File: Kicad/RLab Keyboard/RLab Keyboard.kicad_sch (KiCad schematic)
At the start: 75 parts, among them J1 Conn_01x01_Pin, J10 Conn_01x01_Pin, J11 Conn_01x01_Pin, J12 Conn_01x01_Pin, J13 Conn_01x04, J14 Conn_01x07, J15 Conn_01x03, J16 AudioJack3_Switch, J17 Conn_01x03, J18 Conn_01x03, J19 Conn_01x09, J2 Conn_01x01_Pin, J3 Conn_01x01_Pin, J4 Conn_01x01_Pin, J5 Conn_01x01_Pin, J6 Conn_01x01_Pin, J7 Conn_01x01_Pin, J8 Conn_01x01_Pin, J9 Conn_01x01_Pin, SW1 SW_MEC_5G, SW2 SW_MEC_5G, U1 MPR121QR2, U2 LP5907MFX-3.3, U3 74LVC1G17, U4 PCM5102, U5 LM386

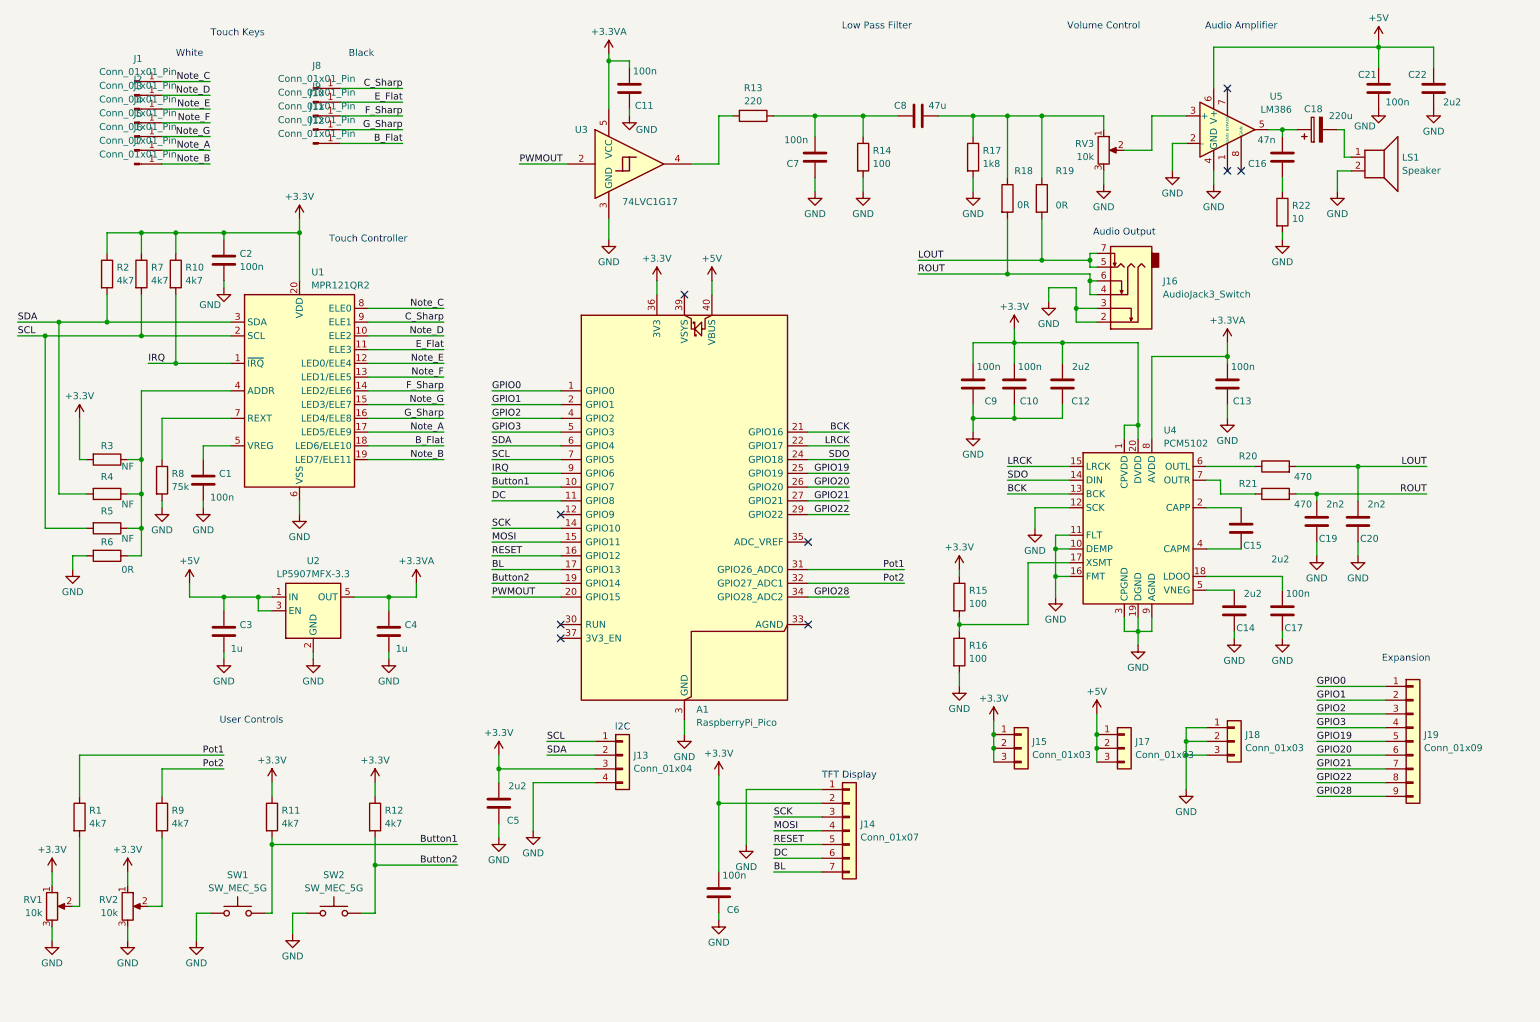
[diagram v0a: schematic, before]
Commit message: Initial submit of version 1.2
Update to layout of Kicad files for new user interface
Added circuit Python test firmware
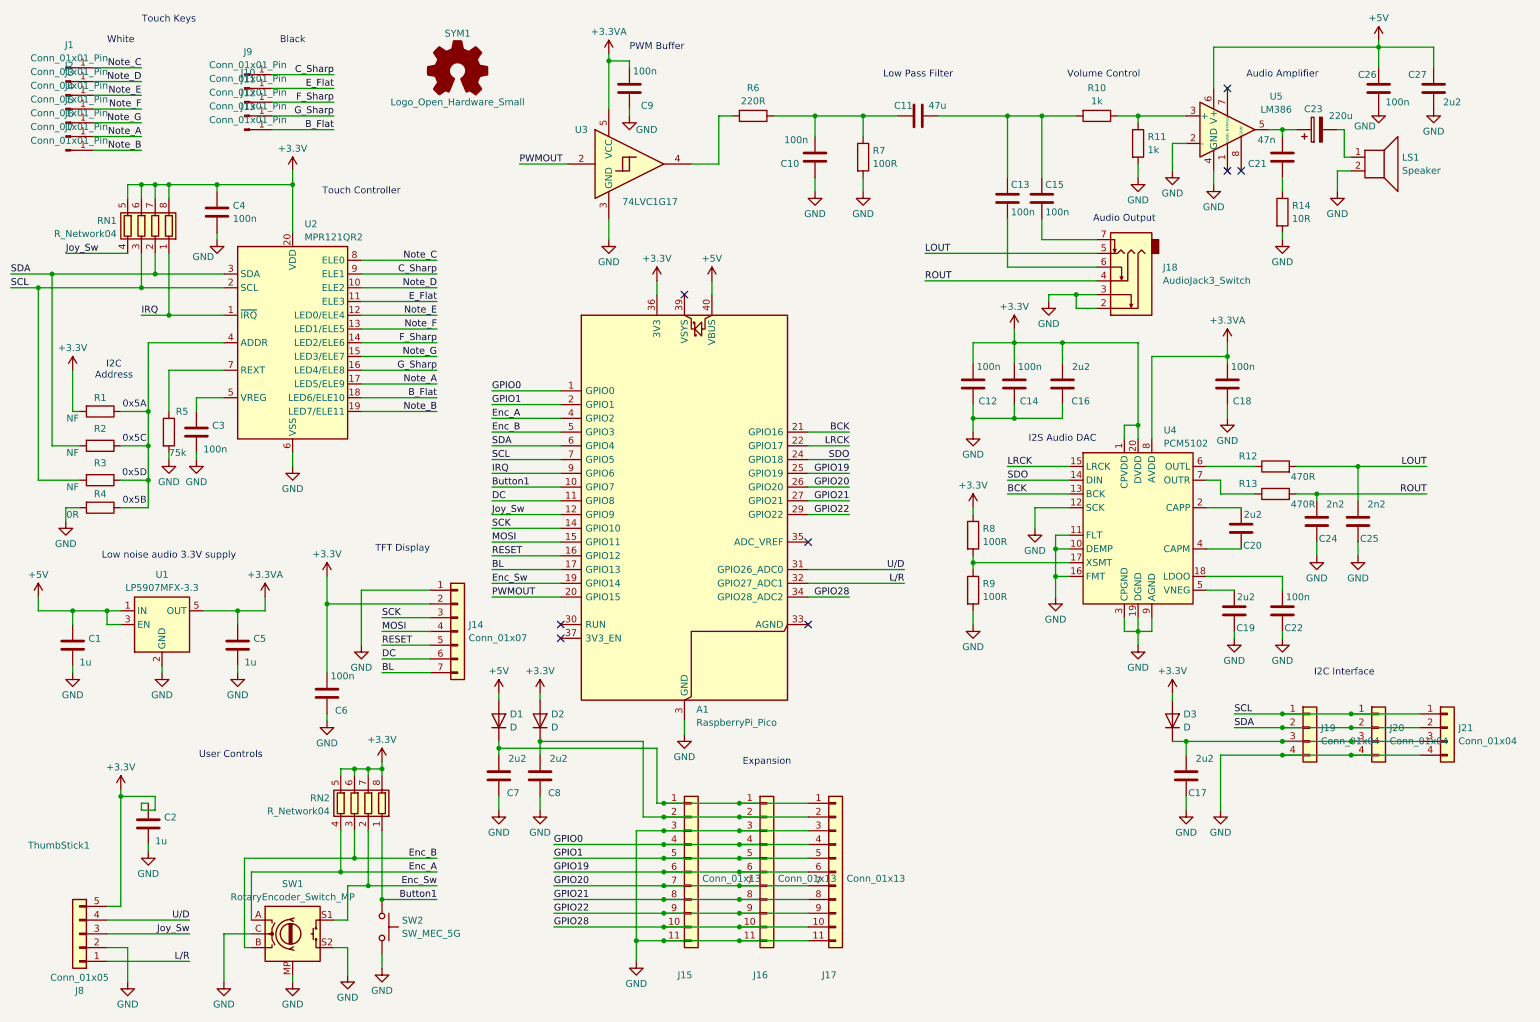
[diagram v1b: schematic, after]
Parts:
- removed J15, J17, J18: Conn_01x03, Connector_PinSocket_2.54mm:PinSocket_1x03_P2.54mm_Vertical, symbol Connector_Generic:Conn_01x03
- removed J19: Conn_01x09, Connector_PinSocket_2.54mm:PinSocket_1x09_P2.54mm_Vertical, symbol Connector_Generic:Conn_01x09
- removed R1, R12, R2, R7, R9: 4k7, Resistor_SMD:R_0603_1608Metric, symbol Device:R
- removed R17: 1k8, Resistor_SMD:R_0603_1608Metric, symbol Device:R
- removed RV1, RV2: 10k, rLab_Keyboard:Potentiometer_Alps_RK09K_Single_Vertical, symbol Device:R_Potentiometer
- removed RV3: 10k, rLab_Keyboard:Potentiometer_Bourns_3214G_Horizontal, symbol Device:R_Potentiometer
- removed SW2: SW_MEC_5G, Button_Switch_THT:SW_PUSH_6mm_H5mm, symbol Switch:SW_Omron_B3FS
- added C2: 1u, Capacitor_SMD:C_0603_1608Metric, symbol Device:C
- added C7, C8: 2u2, Capacitor_SMD:C_0603_1608Metric, symbol Device:C
- added D1, D2, D3: D, Diode_SMD:D_SOD-323, symbol Device:D
- added J15: Conn_01x13, Connector_PinHeader_2.54mm:PinHeader_1x11_P2.54mm_Horizontal, symbol Connector_Generic:Conn_01x11
- added J16: Conn_01x13, Connector_PinSocket_2.54mm:PinSocket_1x11_P2.54mm_Horizontal, symbol Connector_Generic:Conn_01x11
- added J17: Conn_01x13, Connector_PinSocket_2.54mm:PinSocket_1x11_P2.54mm_Vertical, symbol Connector_Generic:Conn_01x11
- added J20: Conn_01x04, Connector_PinSocket_2.54mm:PinSocket_1x04_P2.54mm_Horizontal, symbol Connector_Generic:Conn_01x04
- added J21: Conn_01x04, Connector_PinHeader_2.54mm:PinHeader_1x04_P2.54mm_Horizontal, symbol Connector_Generic:Conn_01x04
- added J8: Conn_01x05, Connector_FFC-FPC:TE_0-1734839-5_1x05-1MP_P0.5mm_Horizontal, symbol Connector_Generic:Conn_01x05
- added RN1, RN2: R_Network04, Resistor_SMD:R_Array_Concave_4x0402, symbol Device:R_Pack04
- added SW1: RotaryEncoder_Switch_MP, rLab_Keyboard:RotaryEncoder_Alps_EC11E-Switch_Vertical_H20mm, symbol Device:RotaryEncoder_Switch_MP
- added SYM1: Logo_Open_Hardware_Small, Symbol:OSHW-Logo_11.4x12mm_SilkScreen, symbol Graphic:Logo_Open_Hardware_Small
- added ThumbStick1: ~, rLab_Keyboard:Thumb_stick, symbol rLab_Keyboard:Thumb_stick
- A1: footprint Pi_Pico2:RPi_Pico_SMD_TH -> rLab_Keyboard:RPi_Pico_SMD_TH
- C13: renamed from R18; value 0R -> 100n; footprint Resistor_SMD:R_0603_1608Metric -> Capacitor_SMD:C_0603_1608Metric; symbol Device:R -> Device:C
- C15: renamed from R19; value 0R -> 100n; footprint Resistor_SMD:R_0603_1608Metric -> Capacitor_SMD:C_0603_1608Metric; symbol Device:R -> Device:C
- J10: renamed from J9; footprint rLab_Keyboard:Black_key -> rLab_Keyboard:Black_key_fill
- J11: renamed from J10; footprint rLab_Keyboard:Black_key -> rLab_Keyboard:Black_key_fill
- J12: renamed from J11; footprint rLab_Keyboard:Black_key -> rLab_Keyboard:Black_key_fill
- J13: renamed from J12; footprint rLab_Keyboard:Black_key -> rLab_Keyboard:Black_key_fill
- J9: renamed from J8; footprint rLab_Keyboard:Black_key -> rLab_Keyboard:Black_key_fill
- R10, R11: value 4k7 -> 1k
- R12: renamed from R20; value 470 -> 470R
- R13: renamed from R21; value 470 -> 470R
- R14: renamed from R22; value 10 -> 10R
- R6: renamed from R13; value 220 -> 220R
- R7: renamed from R14; value 100 -> 100R
- R8: renamed from R15; value 100 -> 100R
- R9: renamed from R16; value 100 -> 100R
- renumbered C3 to C1, C7 to C10, C8 to C11, C9 to C12, C10 to C14, C12 to C16, C5 to C17, C13 to C18, C14 to C19, C15 to C20, C16 to C21, C17 to C22, C18 to C23, C19 to C24, C20 to C25, C21 to C26, C22 to C27, C1 to C3, C2 to C4, C4 to C5, C11 to C9, J16 to J18, J13 to J19, R3 to R1, R4 to R2, R5 to R3, R6 to R4, R8 to R5, SW1 to SW2, U2 to U1, U1 to U2
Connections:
- net +3.3V: now also C2.1, D2.2 (A), D3.2 (A), J8.5 (Pin_5), RN1.5 (R4.2), RN1.6 (R3.2), RN1.7 (R2.2), RN1.8 (R1.2), RN2.5 (R4.2), RN2.6 (R3.2), RN2.7 (R2.2), RN2.8 (R1.2); no longer C17.2, J19.3 (Pin_3), R10.1, R11.1
- net +5V: now also D1.2 (A)
- net Button1: now also SW2.1, RN2.1 (R1.1); no longer R11.2, SW2.2
- net GND: now also R11.2, SW2.2, C2.2, C7.1, C8.1, J15.11 (Pin_11), J15.3 (Pin_3), J16.11 (Pin_11), J16.3 (Pin_3), J17.11 (Pin_11), J17.3 (Pin_3), J20.4 (Pin_4), J21.4 (Pin_4), J8.2 (Pin_2), SW1.C, SW1.MP, SW1.S2; no longer SW2.1
- net GPIO0: now also J15.4 (Pin_4), J16.4 (Pin_4), J17.4 (Pin_4)
- net GPIO1: now also J15.5 (Pin_5), J16.5 (Pin_5), J17.5 (Pin_5)
- net GPIO19: now also J15.6 (Pin_6), J16.6 (Pin_6), J17.6 (Pin_6)
- net GPIO20: now also J15.7 (Pin_7), J16.7 (Pin_7), J17.7 (Pin_7)
- net GPIO21: now also J15.8 (Pin_8), J16.8 (Pin_8), J17.8 (Pin_8)
- net GPIO22: now also J15.9 (Pin_9), J16.9 (Pin_9), J17.9 (Pin_9)
- net GPIO28: now also J15.10 (Pin_10), J16.10 (Pin_10), J17.10 (Pin_10)
- net IRQ: now also RN1.1 (R1.1); no longer R10.2
- net LOUT: no longer C15.2, J18.7
- net ROUT: no longer C13.2, J18.6
- net SCL: now also J20.1 (Pin_1), J21.1 (Pin_1), RN1.3 (R3.1)
- net SDA: now also J20.2 (Pin_2), J21.2 (Pin_2), RN1.2 (R2.1)
- net at C11.1, C13.1, C15.1: now also R10.2
- net at U5.3 (+): now also R10.1, R11.1
- net Joy_Sw: now reaches A1.12 (GPIO9)
- net Joy_Sw: now also J8.3 (Pin_3), RN1.4 (R4.1)
- net Button2 renamed Enc_Sw
- net Enc_Sw: now also RN2.2 (R2.1), SW1.S1
- net GPIO2 renamed Enc_A
- net Enc_A: now also RN2.4 (R4.1), SW1.A
- net GPIO3 renamed Enc_B
- net Enc_B: now also RN2.3 (R3.1), SW1.B
- net Pot1 renamed U/D
- net U/D: now also J8.4 (Pin_4)
- net Pot2 renamed L/R
- net L/R: now also J8.1 (Pin_1)
- new net: C17.2, D3.1 (K), J19.3 (Pin_3), J20.3 (Pin_3), J21.3 (Pin_3)
- new net: C8.2, D2.1 (K), J15.2 (Pin_2), J16.2 (Pin_2), J17.2 (Pin_2)
- new net: C7.2, D1.1 (K), J15.1 (Pin_1), J16.1 (Pin_1), J17.1 (Pin_1)
- new net: C13.2, J18.6
- new net: C15.2, J18.7
- no-connect marks 9 -> 8
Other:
- note added: "0x5A"
- note added: "0x5B"
- note added: "0x5C"
- note added: "0x5D"
- note added: "I2C Address"
- note added: "I2C Interface"
- note added: "I2S Audio DAC"
- note added: "Low noise audio 3.3V supply"
- note added: "PWM Buffer"
- note removed: "I2C"
- moved on the sheet: C1, C17, C3, C4, C5, C6, J1, J10, J11, J12, J13, J14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

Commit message: Latest rLab Keyboard layout
Added connectors for joining boards
Swap display and speaker.
New control layout
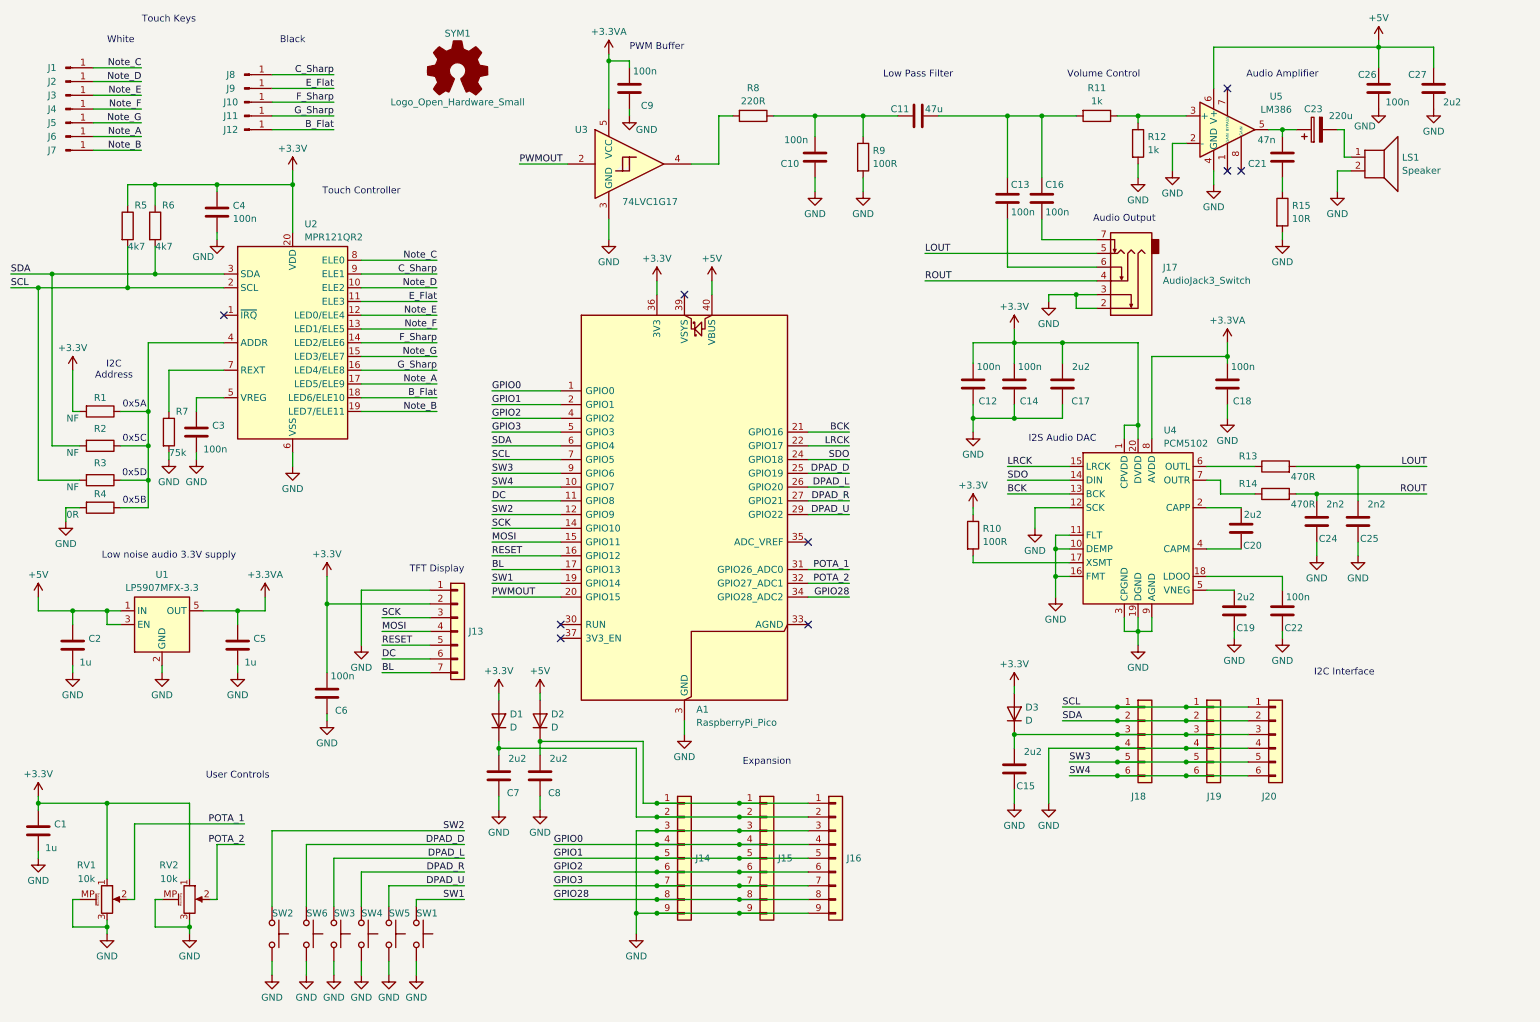
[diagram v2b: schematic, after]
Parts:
- removed J15: Conn_01x13, Connector_PinHeader_2.54mm:PinHeader_1x11_P2.54mm_Horizontal, symbol Connector_Generic:Conn_01x11
- removed J16: Conn_01x13, Connector_PinSocket_2.54mm:PinSocket_1x11_P2.54mm_Horizontal, symbol Connector_Generic:Conn_01x11
- removed J17: Conn_01x13, Connector_PinSocket_2.54mm:PinSocket_1x11_P2.54mm_Vertical, symbol Connector_Generic:Conn_01x11
- removed J19: Conn_01x04, Connector_PinSocket_2.54mm:PinSocket_1x04_P2.54mm_Vertical, symbol Connector_Generic:Conn_01x04
- removed J20: Conn_01x04, Connector_PinSocket_2.54mm:PinSocket_1x04_P2.54mm_Horizontal, symbol Connector_Generic:Conn_01x04
- removed J21: Conn_01x04, Connector_PinHeader_2.54mm:PinHeader_1x04_P2.54mm_Horizontal, symbol Connector_Generic:Conn_01x04
- removed J8: Conn_01x05, Connector_FFC-FPC:TE_0-1734839-5_1x05-1MP_P0.5mm_Horizontal, symbol Connector_Generic:Conn_01x05
- removed R9: 100R, Resistor_SMD:R_0603_1608Metric, symbol Device:R
- removed RN1, RN2: R_Network04, Resistor_SMD:R_Array_Concave_4x0402, symbol Device:R_Pack04
- removed SW1: RotaryEncoder_Switch_MP, rLab_Keyboard:RotaryEncoder_Alps_EC11E-Switch_Vertical_H20mm, symbol Device:RotaryEncoder_Switch_MP
- removed ThumbStick1: ~, rLab_Keyboard:Thumb_stick, symbol rLab_Keyboard:Thumb_stick
- added J14: Conn_01x09, rLab_Keyboard:PinHeader_1x09_P2.54mm_Horizontal, symbol Connector_Generic:Conn_01x09
- added J15: Conn_01x09, Connector_PinSocket_2.54mm:PinSocket_1x09_P2.54mm_Vertical, symbol Connector_Generic:Conn_01x09
- added J16: Conn_01x09, Connector_PinSocket_2.54mm:PinSocket_1x09_P2.54mm_Horizontal, symbol Connector_Generic:Conn_01x09
- added J18: Conn_01x06, Connector_PinSocket_2.54mm:PinSocket_1x06_P2.54mm_Horizontal, symbol Connector_Generic:Conn_01x06
- added J19: Conn_01x06, rLab_Keyboard:PinHeader_1x06_P2.54mm_Horizontal, symbol Connector_Generic:Conn_01x06
- added J20: Conn_01x06, Connector_PinSocket_2.54mm:PinSocket_1x06_P2.54mm_Vertical, symbol Connector_Generic:Conn_01x06
- added R5, R6: 4k7, Resistor_SMD:R_0603_1608Metric, symbol Device:R
- added RV1, RV2: 10k, rLab_Keyboard:Potentiometer_Alps_RK09K_Single_Vertical, symbol Device:R_Potentiometer_MountingPin
- added SW2, SW3, SW4, SW5, SW6: SW_MEC_5G, Button_Switch_THT:SW_PUSH_6mm_H8mm, symbol Switch:SW_Omron_B3FS
- SW1: renamed from SW2; footprint Button_Switch_THT:SW_PUSH_6mm_H5mm -> Button_Switch_THT:SW_PUSH_6mm_H8mm
- renumbered C2 to C1, C17 to C15, C15 to C16, C16 to C17, C1 to C2, J11 to J10, J12 to J11, J13 to J12, J14 to J13, J18 to J17, J9 to J8, J10 to J9, R8 to R10, R10 to R11, R11 to R12, R12 to R13, R13 to R14, R14 to R15, R5 to R7, R6 to R8, R7 to R9
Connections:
- net Enc_Sw is gone; now on net SW1: A1.19 (GPIO14)
- net +3.3V: now also D1.2 (A), R5.1, R6.1, RV1.1, RV2.1; no longer D2.2 (A)
- net +5V: now also D2.2 (A); no longer D1.2 (A)
- net GND: now also J14.3 (Pin_3), J14.9 (Pin_9), J15.3 (Pin_3), J15.9 (Pin_9), J16.3 (Pin_3), J16.9 (Pin_9), J18.4 (Pin_4), J19.4 (Pin_4), J20.4 (Pin_4), RV1.3, RV1.MP (MountPin), RV2.3, RV2.MP (MountPin), SW2.2, SW3.2, SW4.2, SW5.2, SW6.2
- net GPIO0: now also J14.4 (Pin_4), J15.4 (Pin_4), J16.4 (Pin_4)
- net GPIO1: now also J14.5 (Pin_5), J15.5 (Pin_5), J16.5 (Pin_5)
- net GPIO28: now also J14.8 (Pin_8), J15.8 (Pin_8), J16.8 (Pin_8)
- net SCL: now also J18.1 (Pin_1), J19.1 (Pin_1), J20.1 (Pin_1), R5.2
- net SDA: now also J18.2 (Pin_2), J19.2 (Pin_2), J20.2 (Pin_2), R6.2
- net at C15.2, D3.1 (K): now also J18.3 (Pin_3), J19.3 (Pin_3), J20.3 (Pin_3)
- net at C8.2, D2.1 (K): now also J14.1 (Pin_1), J15.1 (Pin_1), J16.1 (Pin_1)
- net at C7.2, D1.1 (K): now also J14.2 (Pin_2), J15.2 (Pin_2), J16.2 (Pin_2)
- net Button1 renamed SW1
- net SW1: no longer A1.10 (GPIO7)
- net Enc_A renamed GPIO2
- net GPIO2: now also J14.6 (Pin_6), J15.6 (Pin_6), J16.6 (Pin_6)
- net Enc_B renamed GPIO3
- net GPIO3: now also J14.7 (Pin_7), J15.7 (Pin_7), J16.7 (Pin_7)
- net GPIO19 renamed DPAD_D
- net DPAD_D: now also SW6.1
- net GPIO20 renamed DPAD_L
- net DPAD_L: now also SW3.1
- net GPIO21 renamed DPAD_R
- net DPAD_R: now also SW4.1
- net GPIO22 renamed DPAD_U
- net DPAD_U: now also SW5.1
- net IRQ: no longer names the net of U2.1 (~{IRQ})
- net IRQ: no longer A1.9 (GPIO6)
- net Joy_Sw renamed SW2
- net SW2: now also SW2.1
- net L/R renamed POTA_2
- net POTA_2: now also RV2.2
- net U/D renamed POTA_1
- net POTA_1: now also RV1.2
- new net SW3: A1.9 (GPIO6), J18.5 (Pin_5), J19.5 (Pin_5), J20.5 (Pin_5)
- new net SW4: A1.10 (GPIO7), J18.6 (Pin_6), J19.6 (Pin_6), J20.6 (Pin_6)
- no-connect marks 8 -> 9
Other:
- moved on the sheet: C1, C15, D3, SW1
